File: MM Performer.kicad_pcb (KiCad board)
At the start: 2 copper layers, 39 parts, among them IC1 MC68000P, U1 MC68030RC, U2 MC68881FN-SOC, U3 ATF16V8BJ, U4 ATF16V8BJ, U5 ATF16V8BJ, U6 ATF16V8BJ, U7 ATF16V8BJ

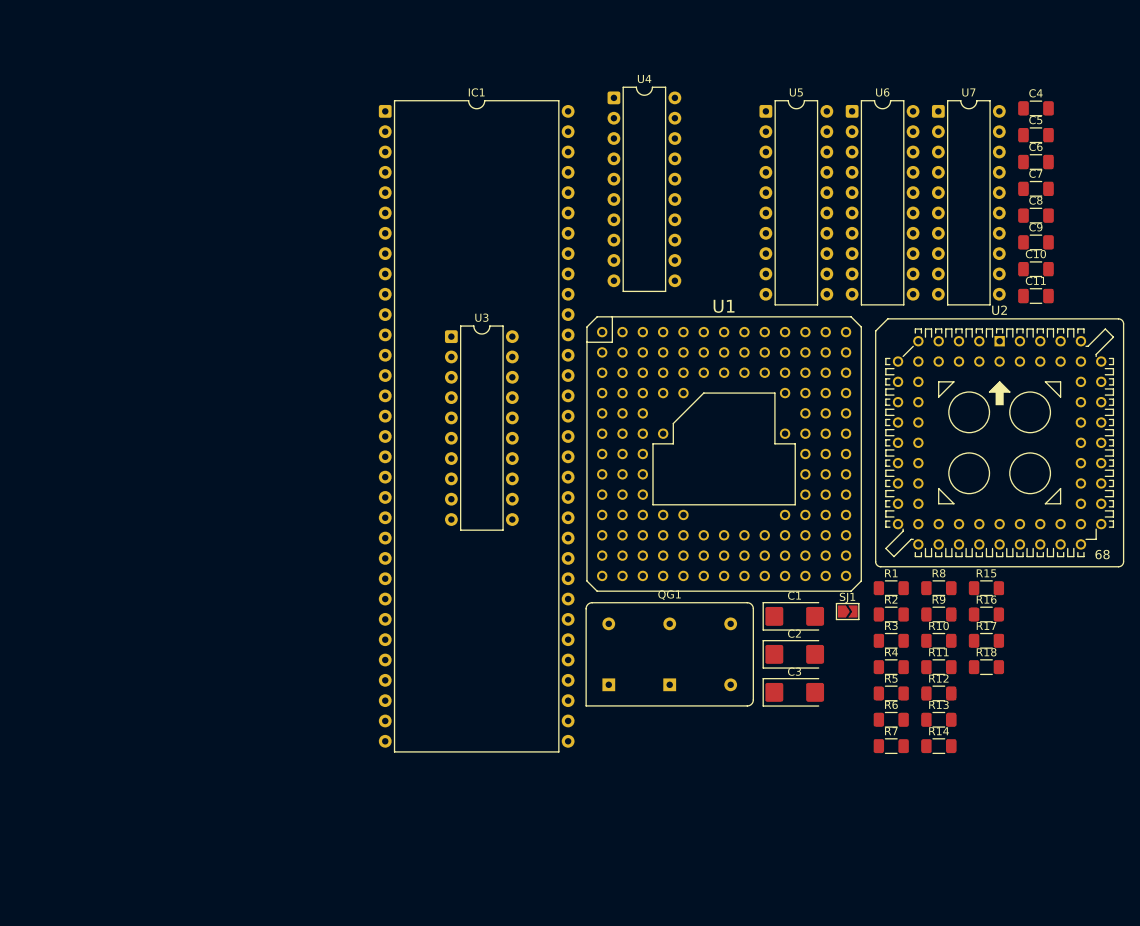
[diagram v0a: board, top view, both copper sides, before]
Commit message: Tweak positioning a bit
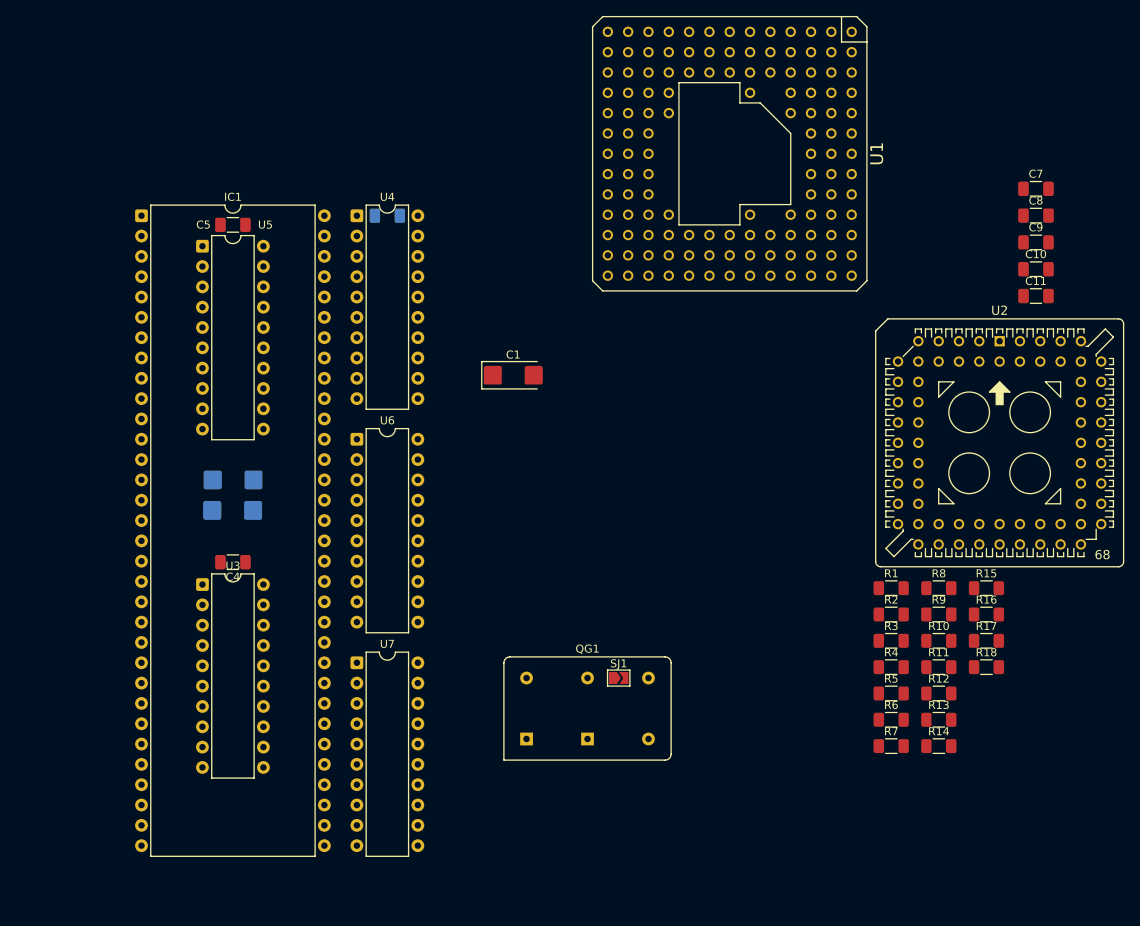
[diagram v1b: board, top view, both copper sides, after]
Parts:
- C1: value 22uF/10V -> 22uF
- C2, C3: value 22uF/10V -> 22uF; moved to B.Cu
- C6: moved to B.Cu
- IC1: value MC68000P -> 68000D
- moved C4 115.3 mm to (50.2, 99.2), turned to 180 degrees
- moved C5 101.0 mm to (50.2, 57.0), turned to 180 degrees
- moved U7 100.2 mm to (65.7, 111.8)
- moved C6 81.4 mm to (69.5, 55.9), turned to 180 degrees
- moved C3 75.1 mm to (50.2, 88.9)
- moved U6 74.2 mm to (65.7, 83.8)
- moved C2 72.5 mm to (50.1, 92.7), turned to 180 degrees
- moved U5 72.4 mm to (46.4, 59.7)
- moved C1 46.3 mm to (85.2, 75.8)
- moved U3 43.9 mm to (46.4, 102.0)
- moved U1 37.5 mm to (112.3, 48.1), turned to -90 degrees
- moved U4 35.3 mm to (65.7, 55.9)
- moved IC1 33.1 mm to (38.7, 55.9)
- moved SJ1 29.8 mm to (98.4, 113.7)
- moved QG1 12.3 mm to (86.9, 121.3)
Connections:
- C1 pad 1: (no net) -> VCC
- C1 pad 2: (no net) -> GND
- C2 pad 1: (no net) -> VCC
- C2 pad 2: (no net) -> GND
- C3 pad 1: (no net) -> VCC
- C3 pad 2: (no net) -> GND
- IC1 pad 14: (no net) -> VCC
- IC1 pad 16: (no net) -> GND
- IC1 pad 49: (no net) -> VCC
- IC1 pad 53: (no net) -> GND

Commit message: Reorganize a bit
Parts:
- C10: moved to B.Cu
- C6: moved to F.Cu
- U3, U4, U5, U6: footprint Package_DIP:DIP-20_W7.62mm -> footprints:PLCC-20_THT-Socket
- moved C9 115.3 mm to (50.1, 115.8), turned to 180 degrees
- moved C8 108.1 mm to (50.1, 96.0), turned to 180 degrees
- moved C7 103.2 mm to (50.1, 76.2), turned to 180 degrees
- moved C11 96.3 mm to (87.5, 138.7), turned to 90 degrees
- moved C10 79.0 mm to (73.2, 78.5), turned to 90 degrees
- moved U1 76.9 mm to (81.8, 118.7)
- moved U2 68.9 mm to (80.4, 92.6), turned to 180 degrees
- moved R11 64.8 mm to (79.2, 138.7), turned to -90 degrees
- moved R7 62.9 mm to (74.0, 98.8), turned to 90 degrees
- moved R12 59.3 mm to (83.8, 138.7), turned to -90 degrees
- moved R3 58.9 mm to (81.5, 138.7), turned to -90 degrees
- moved SJ1 55.0 mm to (58.5, 75.8)
- moved QG1 51.9 mm to (99.8, 71.0), turned to -90 degrees
- moved U7 49.8 mm to (65.9, 62.0), turned to 90 degrees
- moved C6 48.6 mm to (117.8, 60.3), turned to 0 degrees
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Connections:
- U1 pad D10: (no net) -> VCC
- U1 pad E11: (no net) -> GND
- U1 pad F11: (no net) -> VCC
- U1 pad G11: (no net) -> GND
- U1 pad H11: (no net) -> VCC
- U1 pad J11: (no net) -> GND
- U1 pad K10: (no net) -> VCC
- U2 pad 10: (no net) -> VCC
- U2 pad 12: (no net) -> GND
- U2 pad 14: (no net) -> GND
- U2 pad 16: (no net) -> VCC
- U2 pad 17: (no net) -> VCC
- U2 pad 19: (no net) -> GND
- U2 pad 27: (no net) -> VCC
- U2 pad 30: (no net) -> GND
- U2 pad 41: (no net) -> GND
- U2 pad 43: (no net) -> VCC
- U2 pad 5: (no net) -> GND
- U2 pad 51: (no net) -> GND
- U2 pad 52: (no net) -> VCC
- U2 pad 53: (no net) -> VCC
- U2 pad 6: (no net) -> GND
- U2 pad 61: (no net) -> VCC
- U2 pad 63: (no net) -> GND
- U2 pad 7: (no net) -> GND
- U2 pad 8: (no net) -> GND
- U2 pad 9: (no net) -> GND

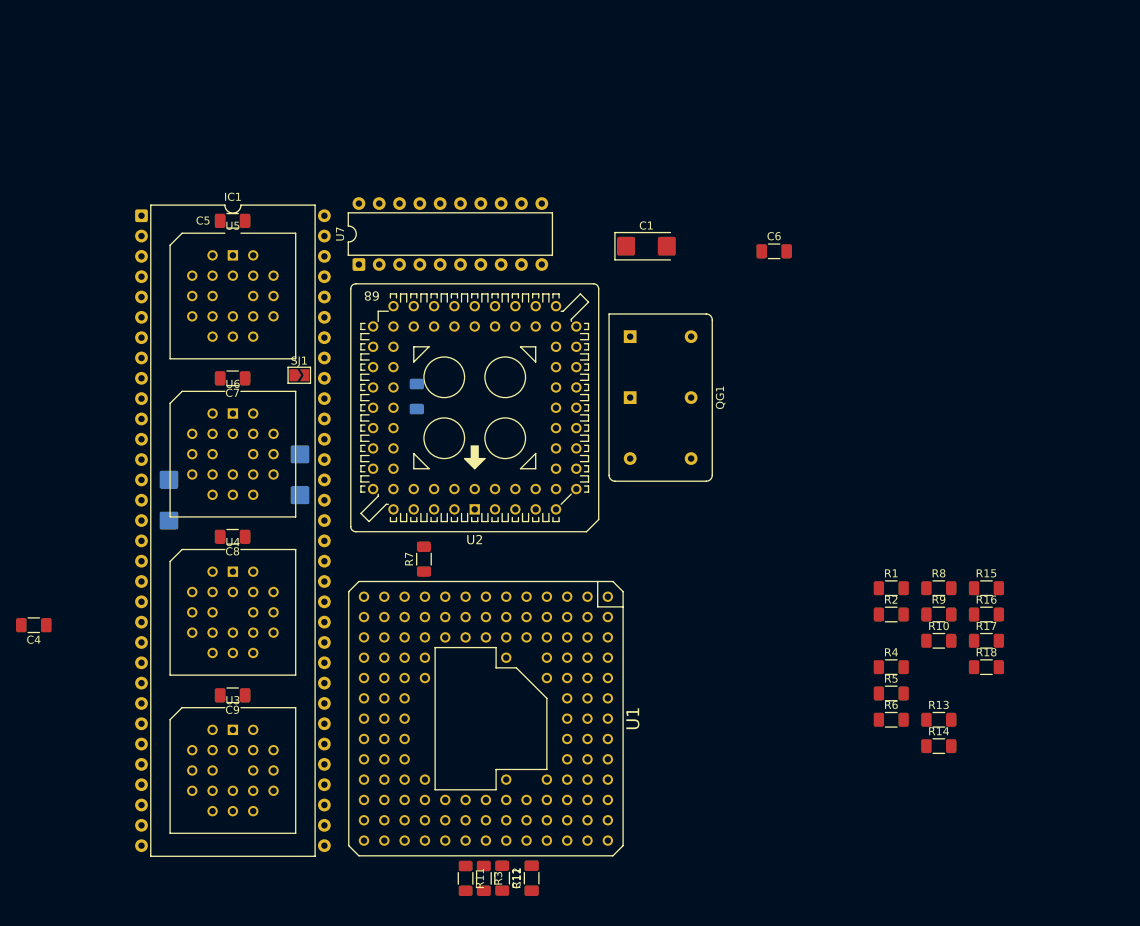
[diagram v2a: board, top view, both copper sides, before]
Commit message: Reorganize the positions
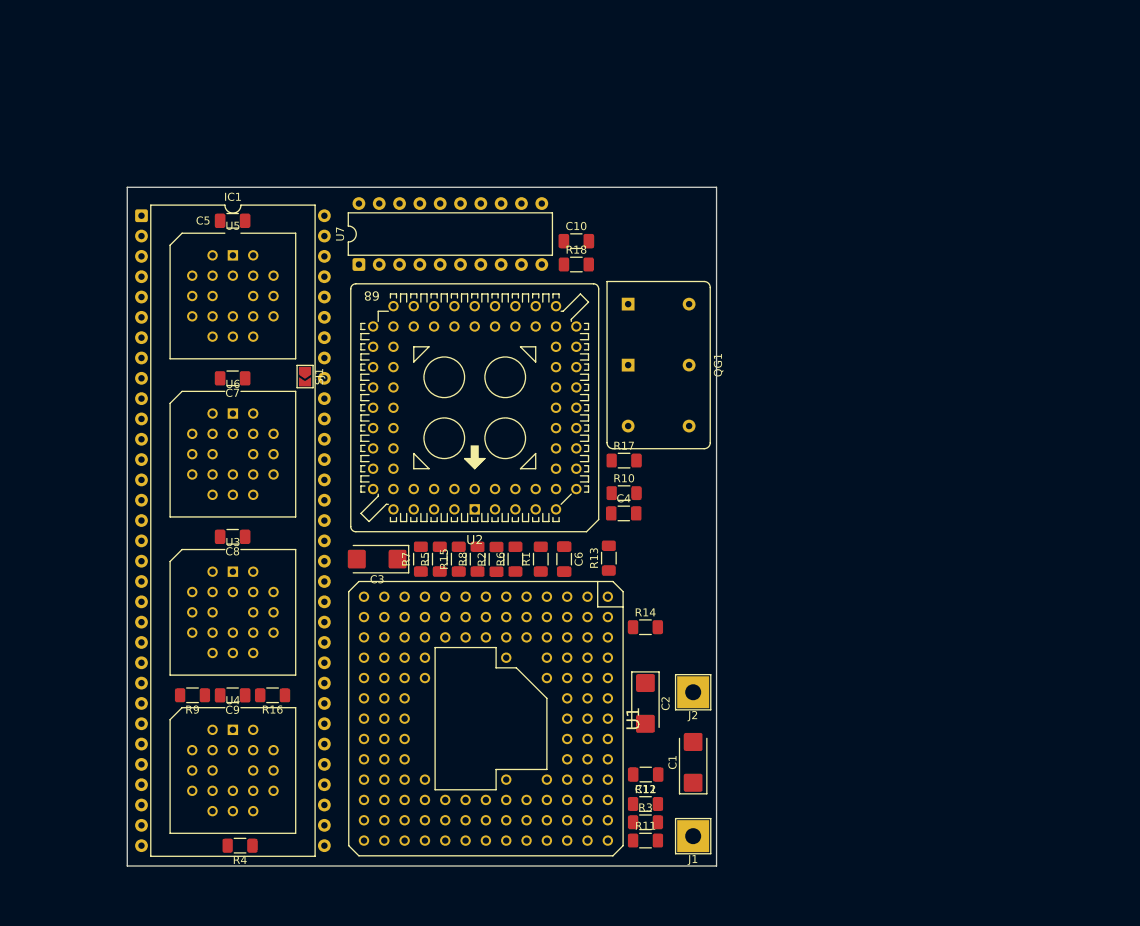
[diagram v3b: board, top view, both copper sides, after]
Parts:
- added J1: VCC, TestPoint:TestPoint_THTPad_4.0x4.0mm_Drill2.0mm, F.Cu at (107.7, 133.4)
- added J2: GND, TestPoint:TestPoint_THTPad_4.0x4.0mm_Drill2.0mm, F.Cu at (107.7, 115.4)
- C10, C2, C3: moved to F.Cu
- moved R9 93.8 mm to (45.1, 115.8), turned to 180 degrees
- moved R16 89.8 mm to (55.1, 115.8), turned to 180 degrees
- moved R4 84.4 mm to (51.1, 134.6), turned to 180 degrees
- moved C4 75.1 mm to (99.0, 93.1), turned to 0 degrees
- moved R18 71.8 mm to (93.1, 62.0)
- moved R15 66.1 mm to (78.4, 98.8), turned to 90 degrees
- moved C1 64.8 mm to (107.7, 124.2), turned to 90 degrees
- moved R5 58.9 mm to (76.0, 98.8), turned to 90 degrees
- moved R8 57.8 mm to (80.7, 98.8), turned to 90 degrees
- moved C2 51.8 mm to (101.7, 116.8), turned to -90 degrees
- moved R6 51.1 mm to (85.5, 98.8), turned to 90 degrees
- moved R17 50.6 mm to (99.1, 86.5)
- moved R2 49.8 mm to (83.1, 98.8), turned to 90 degrees
- moved C6 46.6 mm to (91.6, 98.8), turned to -90 degrees
- moved R13 45.9 mm to (97.2, 98.7), turned to 90 degrees
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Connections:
- U1 pad A1: (no net) -> //BR_30
- U1 pad A2: (no net) -> /A0
- U1 pad A3: (no net) -> unconnected-(U1A-A30-PadA3)
- U1 pad A4: (no net) -> unconnected-(U1A-A28-PadA4)
- U1 pad A5: (no net) -> unconnected-(U1A-A26-PadA5)
- U1 pad A6: (no net) -> unconnected-(U1A-A24-PadA6)
- U1 pad A7: (no net) -> /A23
- U1 pad A8: (no net) -> /A21
- U1 pad A9: (no net) -> /A19
- U1 pad B1: (no net) -> unconnected-(U1A-RMC-PadB1)
- U1 pad B2: (no net) -> unconnected-(U1A-BG-PadB2)
- U1 pad B3: (no net) -> unconnected-(U1A-A31-PadB3)
- U1 pad B4: (no net) -> unconnected-(U1A-A29-PadB4)
- U1 pad B5: (no net) -> unconnected-(U1A-A27-PadB5)
- U1 pad B6: (no net) -> unconnected-(U1A-A25-PadB6)
- U1 pad B7: (no net) -> /A22
- U1 pad B8: (no net) -> /A20
- U1 pad B9: (no net) -> /A16
- U1 pad C1: (no net) -> /FC1
- U1 pad C2: (no net) -> unconnected-(U1A-CIOUT-PadC2)
- U1 pad C3: (no net) -> //BGACK_30
- U1 pad C4: (no net) -> /A1
- U1 pad C8: (no net) -> /A18
- U1 pad D1: (no net) -> /FC2
- U1 pad D2: (no net) -> /FC0
- U1 pad D3: (no net) -> unconnected-(U1A-OCS-PadD3)
- U1 pad D5: (no net) -> unconnected-(U1A-NC-PadD5)
- U1 pad E1: (no net) -> /CLK_30
- U1 pad E12: (no net) -> unconnected-(U1A-NC-PadE12)
- U1 pad E2: (no net) -> /AVEC
- U1 pad F1: (no net) -> //DSACK0
- U1 pad F10: (no net) -> unconnected-(U1A-NC-PadF10)
- U1 pad F4: (no net) -> unconnected-(U1A-NC-PadF4)
- U1 pad G1: (no net) -> //STERM
- U1 pad G2: (no net) -> //DSACK1
- U1 pad H1: (no net) -> //BERR_30
- U1 pad H2: (no net) -> //HALT_30
- U1 pad J1: (no net) -> //CBACK
- U1 pad J2: (no net) -> //AS_30
- U1 pad K1: (no net) -> unconnected-(U1A-CBREQ-PadK1)
- U1 pad K2: (no net) -> //DS_30
- U1 pad K3: (no net) -> /SIZ1
- U1 pad K5: (no net) -> unconnected-(U1A-NC-PadK5)
- U1 pad L1: (no net) -> //CIIN
- U1 pad L2: (no net) -> /SIZ0
- U1 pad L3: (no net) -> //R/W
- U1 pad L4: (no net) -> /D30
- U1 pad M1: (no net) -> unconnected-(U1A-DBEN-PadM1)
- U1 pad M2: (no net) -> /ECS
- U1 pad M3: (no net) -> /D29
- U1 pad M4: (no net) -> /D27
- U1 pad M5: (no net) -> /D24
- U1 pad M6: (no net) -> /D22
- U1 pad M7: (no net) -> /D20
- U1 pad M8: (no net) -> /D17
- U1 pad M9: (no net) -> /D14
- U1 pad N1: (no net) -> /D31
- U1 pad N2: (no net) -> /D28
- U1 pad N3: (no net) -> /D26
- U1 pad N4: (no net) -> /D25
- U1 pad N5: (no net) -> /D23
- U1 pad N6: (no net) -> /D21
- U1 pad N7: (no net) -> /D19
- U1 pad N8: (no net) -> /D18
- U1 pad N9: (no net) -> /D16
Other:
- board outline added: 73.7 x 84.8 mm
- copper layers 2 -> 4

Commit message: Current setup
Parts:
- moved C2 58.4 mm to (102.5, 58.4), turned to 0 degrees
- moved C3 35.1 mm to (103.3, 99.1), turned to 90 degrees
- moved C10 24.9 mm to (68.2, 58.2), turned to -90 degrees
- moved U3 19.8 mm to (50.2, 120.1)
- moved U4 19.8 mm to (50.2, 100.4)
- moved R4 19.2 mm to (55.1, 115.8)
- moved R9 19.1 mm to (47.7, 134.7), turned to 0 degrees
- moved R16 19.1 mm to (52.7, 134.7)
- moved R18 7.88 mm to (101.0, 61.6)
- moved U7 5.08 mm to (71.0, 62.0)
- moved R5 2.36 mm to (73.7, 98.8)
- moved R7 2.36 mm to (76.0, 98.8)
- moved U2 0.52 mm to (80.5, 92.1)
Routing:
- net VCC: track 0.00 -> 634.5 mm, vias 0 -> 9
- net GND: track 0.00 -> 542.5 mm, vias 0 -> 10
- net /FPUA0: track 0.00 -> 12.6 mm
- net //BGACK_30: track 0.00 -> 8.76 mm
- net /P2.A17: track 0.00 -> 8.75 mm
- net Net-(U7-I5): track 0.00 -> 8.67 mm
- net Net-(U7-I3): track 0.00 -> 8.67 mm
- net Net-(U7-I4): track 0.00 -> 8.67 mm
- net /P3.B10: track 0.00 -> 7.66 mm
- net //DSACK1: track 0.00 -> 7.00 mm
- net //AS_30: track 0.00 -> 6.95 mm
- net //HALT_30: track 0.00 -> 6.53 mm
- net //DSACK0: track 0.00 -> 6.35 mm
- net //EXT.DTK: track 0.00 -> 5.90 mm
- net //STERM: track 0.00 -> 5.20 mm
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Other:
- board size 73.7 x 84.8 mm -> 74.8 x 84.8 mm

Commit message: Performer
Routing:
- net //RESET_30: track 0.00 -> 158.0 mm, vias 0 -> 4
- net VCC: track 634.5 -> 768.6 mm
- net /D17: track 0.00 -> 130.1 mm, vias 0 -> 2
- net /D20: track 0.00 -> 127.7 mm, vias 0 -> 5
- net /A1: track 0.00 -> 127.7 mm, vias 0 -> 4
- net /A4: track 0.00 -> 127.4 mm, vias 0 -> 2
- net //R/W: track 0.00 -> 126.9 mm
- net /A3: track 0.00 -> 123.8 mm, vias 0 -> 4
- net /A2: track 0.00 -> 120.8 mm, vias 0 -> 2
- net /A22: track 0.00 -> 119.9 mm, vias 0 -> 2
- net /D16: track 0.00 -> 119.8 mm, vias 0 -> 1
- net //IPL2: track 0.00 -> 113.1 mm, vias 0 -> 1
- net //FPUCS: track 0.00 -> 106.2 mm, vias 0 -> 2
- net //AS_30: track 6.95 -> 108.7 mm
- net /D18: track 0.00 -> 95.7 mm, vias 0 -> 2
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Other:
- board text added: "MiniPerformer+ Rev. 0"

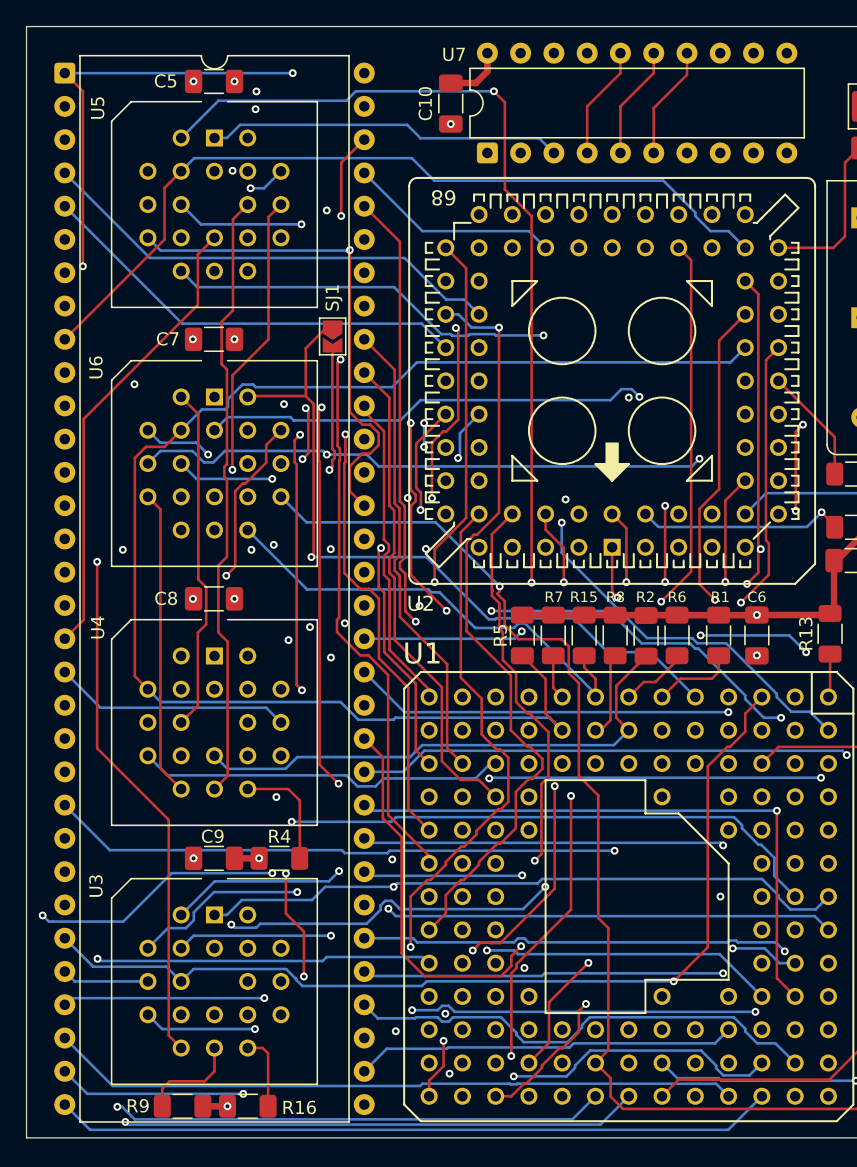
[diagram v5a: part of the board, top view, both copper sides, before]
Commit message: Update footprints
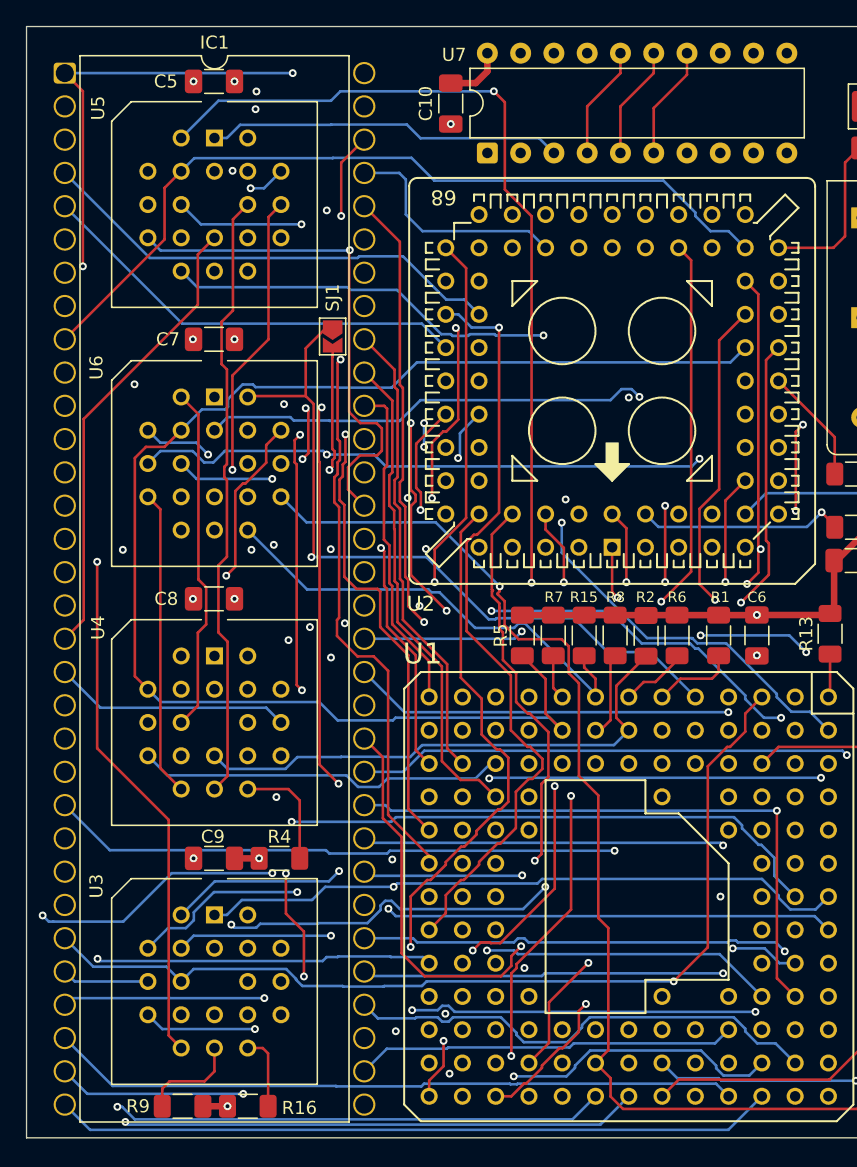
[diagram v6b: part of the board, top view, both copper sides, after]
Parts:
- IC1: footprint Package_DIP:DIP-64_W22.86mm -> footprints:DIP-64_W22.86mm
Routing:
- net VCC: track 768.6 -> 749.4 mm
- net /A21: track 80.1 -> 83.0 mm
- net //FPUCS: track 106.2 -> 108.9 mm
- net /D24: track 75.8 -> 77.4 mm
- net /D3: track 66.5 -> 67.7 mm
- net /A22: track 119.9 -> 121.0 mm
- net /A23: track 82.3 -> 83.2 mm
- net /D23: track 74.4 -> 75.2 mm
- net /D31: track 59.5 -> 60.3 mm
- net /D21: track 77.7 -> 78.3 mm
